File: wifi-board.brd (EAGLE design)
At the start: 50 x 50 mm, 25 parts

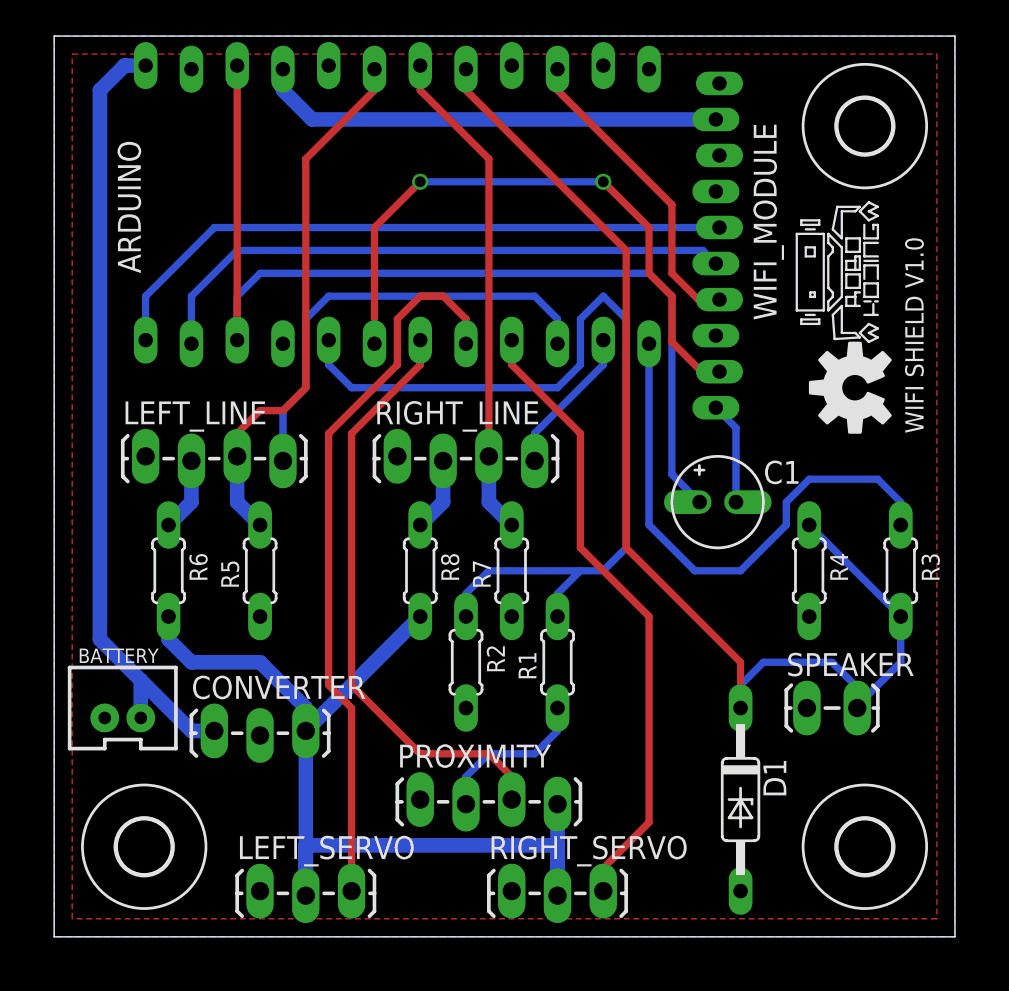
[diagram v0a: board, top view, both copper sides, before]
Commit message: updated battery connector
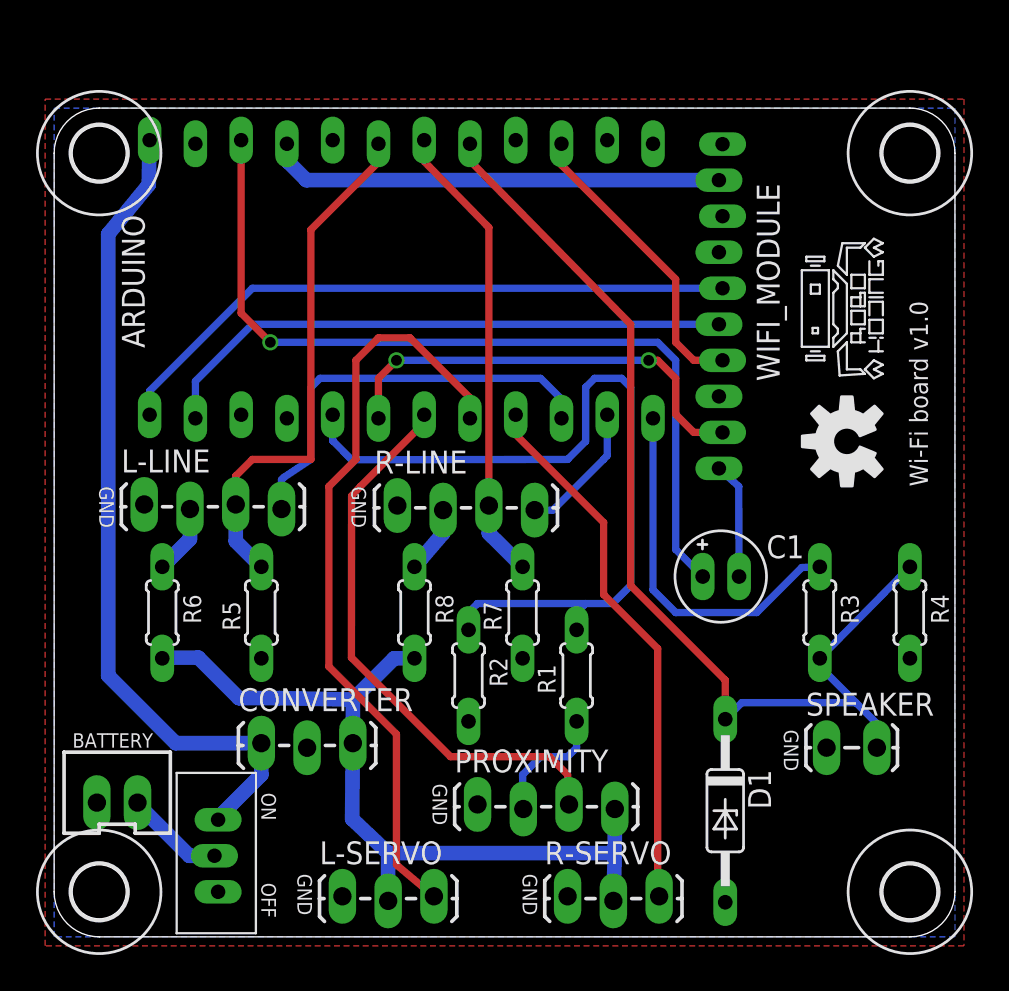
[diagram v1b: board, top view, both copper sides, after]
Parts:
- removed LEFT_LINE, RIGHT_LINE: (no value), SparkFun-Connectors:1X04_LOCK_LONGPADS
- removed LEFT_SERVO, RIGHT_SERVO: (no value), SparkFun-Connectors:1X03_LOCK_LONGPADS
- added L-LINE, R-LINE: (no value), SparkFun-Connectors:1X04_LOCK_LONGPADS
- added L-SERVO, R-SERVO: (no value), SparkFun-Connectors:1X03_LOCK_LONGPADS
- added LOGO2: ROBOKODING-LOGOM, Sumorobot:ROBOKODING-LOGO-M
- added POWER: SPDT_SLIDE_SWITCH, custom:SPDT_SLIDE_SWITCH
- U$4: device Sumorobot:ROBOKODING-LOGO-S -> holes:3,0
- moved U$4 44.5 mm to (2.50, 43.5), turned to 0 degrees
- moved R4 6.05 mm to (47.5, 18.0)
- moved R3 5.05 mm to (42.5, 18.0)
- moved BATTERY 4.71 mm to (3.50, 8.00)
- moved ARDUINO 4.15 mm to (18.0, 36.5)
- moved C1 4.13 mm to (37.0, 20.0)
- moved U$1 3.54 mm to (47.5, 2.50)
- moved U$3 3.54 mm to (2.50, 2.50)
- moved WIFI_MODULE 3.37 mm to (37.0, 36.0)
- moved PROXIMITY 3.19 mm to (23.5, 7.35)
- moved LOGO1 3.01 mm to (44.0, 27.5)
- moved U$2 2.92 mm to (47.5, 43.5)
- moved CONVERTER 2.70 mm to (11.5, 10.8)
- moved SPEAKER 2.46 mm to (43.0, 10.5)
- moved R7 2.40 mm to (26.0, 18.0)
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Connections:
- new net BAT_IN: BATTERY.2, POWER.COMMON
- net +5V: now also L-SERVO.2, R-SERVO.2; no longer LEFT_SERVO.2, RIGHT_SERVO.2
- net A1: now also R-LINE.3; no longer RIGHT_LINE.3
- net A2: now also L-LINE.3; no longer LEFT_LINE.3
- net D5: now also L-SERVO.3; no longer LEFT_SERVO.3
- net D6: now also R-SERVO.3; no longer RIGHT_SERVO.3
- net D7: now also L-LINE.4; no longer LEFT_LINE.4
- net D8: now also R-LINE.4; no longer RIGHT_LINE.4
- net GND: now also L-LINE.1, L-SERVO.1, R-LINE.1, R-SERVO.1; no longer LEFT_LINE.1, LEFT_SERVO.1, RIGHT_LINE.1, RIGHT_SERVO.1
- net N$6: now also L-LINE.2; no longer LEFT_LINE.2
- net N$7: now also R-LINE.2; no longer RIGHT_LINE.2
- net RST: no longer ARDUINO.3
- net VIN: now also POWER.SW2; no longer BATTERY.2
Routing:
- net D3: track 34.0 -> 24.6 mm
- net D9: track 29.7 -> 20.3 mm
- net +5V: track 54.5 -> 45.6 mm
- net RST: track 54.9 -> 47.4 mm, vias 0 -> 1
- net A0: track 65.2 -> 58.8 mm
- net BAT_IN: track 0.00 -> 5.72 mm
- net D6: track 34.8 -> 30.1 mm
- net D2: track 49.5 -> 45.5 mm
- net D5: track 40.1 -> 42.3 mm
- net N$1: track 8.93 -> 6.99 mm
- net VIN: track 44.1 -> 45.9 mm
- net A1: track 27.6 -> 25.9 mm
- net D7: track 24.8 -> 23.3 mm
- net D4: track 33.0 -> 31.5 mm
- net NLINK: track 5.70 -> 6.49 mm
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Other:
- board size 50 x 50 mm -> 50 x 46 mm
- board text added: "GND"
- board text added: "OFF"
- board text added: "ON"
- board text added: "Wi-Fi board v1.0"
- board text removed: "WIFI SHIELD V1.0"
